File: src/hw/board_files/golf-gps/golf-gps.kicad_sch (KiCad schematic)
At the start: 33 parts, among them J1 Micro_SD_Card, J4 Conn_02x03_Top_Bottom, SW2 RESET, SW3 BTN_1, SW4 BTN_2, U1 NEO-M9N, U4 STM32L432KCU6, Y2 32.768kHz

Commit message: Added BOM file, finishing sch
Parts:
- removed C10: 2u2, symbol Device:C_Small
- removed C11, C16, C17, C8, C9: 100n, symbol Device:C_Small
- removed C12, C13: TBD, symbol Device:C_Small
- removed D2: LED_PWR, symbol Device:LED
- removed D4: LED_STATUS, symbol Device:LED
- removed J4: Conn_02x03_Top_Bottom, symbol Connector_Generic:Conn_02x03_Top_Bottom
- removed R11, R6: 330R, symbol Device:R_US
- removed R12, R13, R5: 10k, symbol Device:R_US
- removed SW2: RESET, symbol Switch:SW_Push
- removed SW3: BTN_1, symbol Switch:SW_Push
- removed SW4: BTN_2, symbol Switch:SW_Push
- removed U4: STM32L432KCU6, Package_DFN_QFN:QFN-32-1EP_5x5mm_P0.5mm_EP3.45x3.45mm, symbol MCU_ST_STM32L4:STM32L432KCUx
- removed Y2: 32.768kHz, symbol Device:Crystal_Small
- renumbered C3 to C1, C4 to C2, C2 to C3, J2 to J1, J1 to J2
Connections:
- net LCD_RES is gone; now on net +3V3: J1.4 (RES)
- net ANT: no longer names the net of AE1.1 (A), U1.11 (RF_IN)
- net V_BAT renamed V_BCKP
- no-connect marks 16 -> 9
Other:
- added sheet Microcontroller (microcontroller.kicad_sch)
- note added: "Golf GPS"
- note removed: "Add programming headers"
- note removed: "Buttons"
- note removed: "LEDs"
- note removed: "Pull high?"
- note removed: "STM32 Microcontroller"
- note removed: "SWD Programming Header"
- company: (none) -> Brady Kuhn
- title: (none) -> Golf GPS

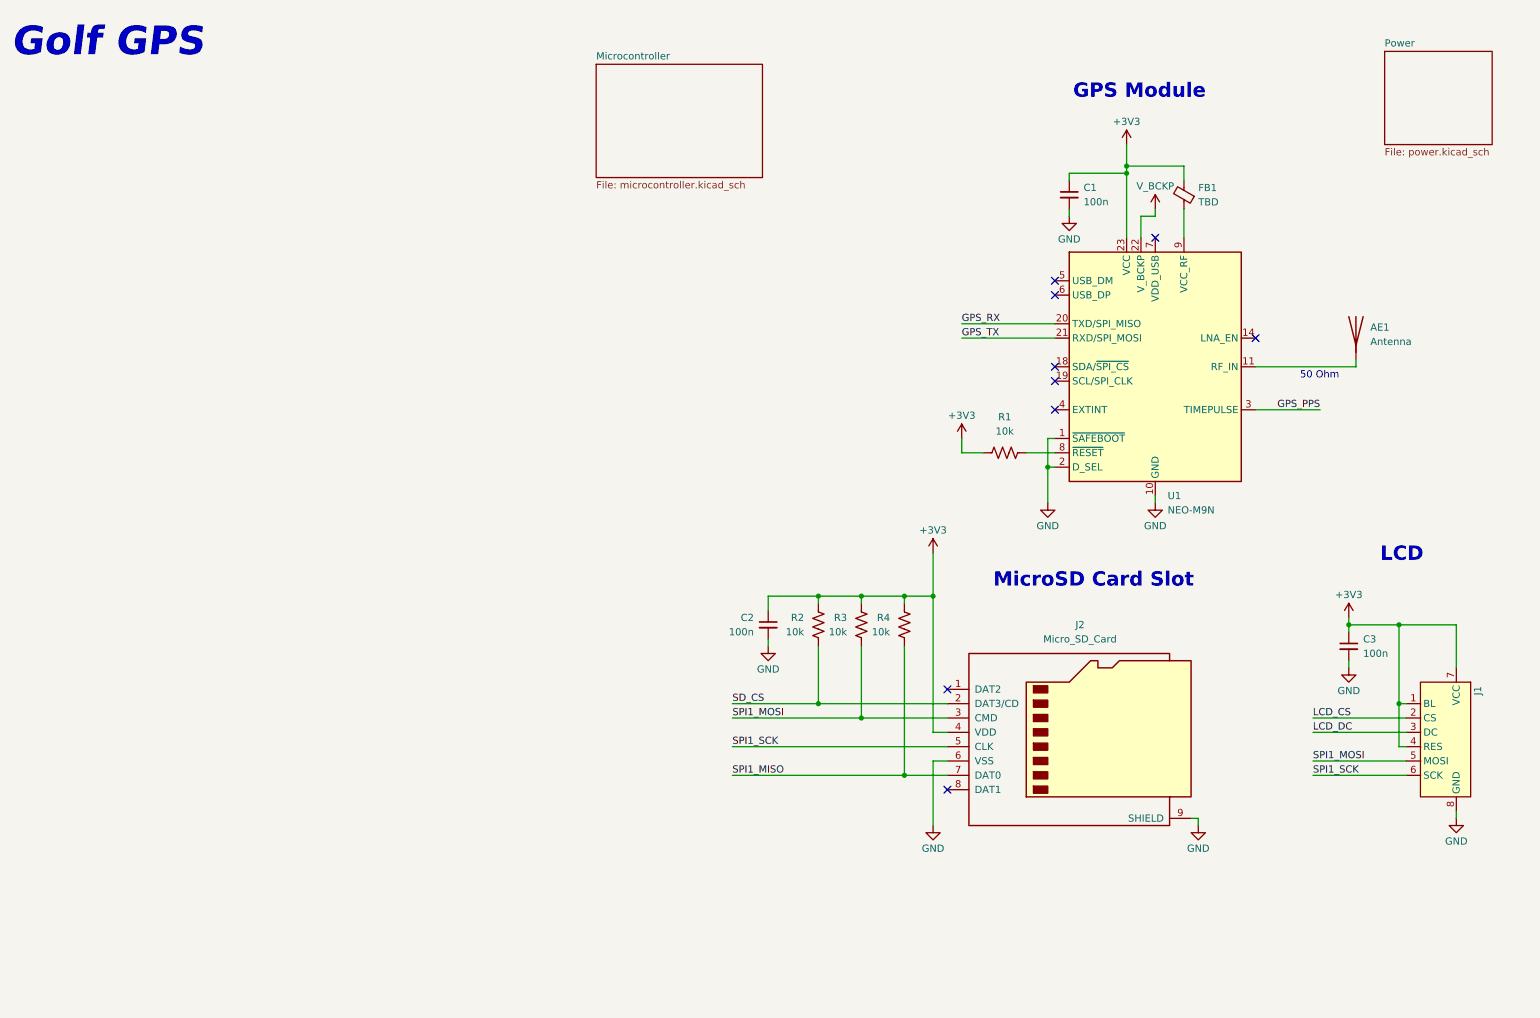
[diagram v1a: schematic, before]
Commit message: Added PI filter to antenna.
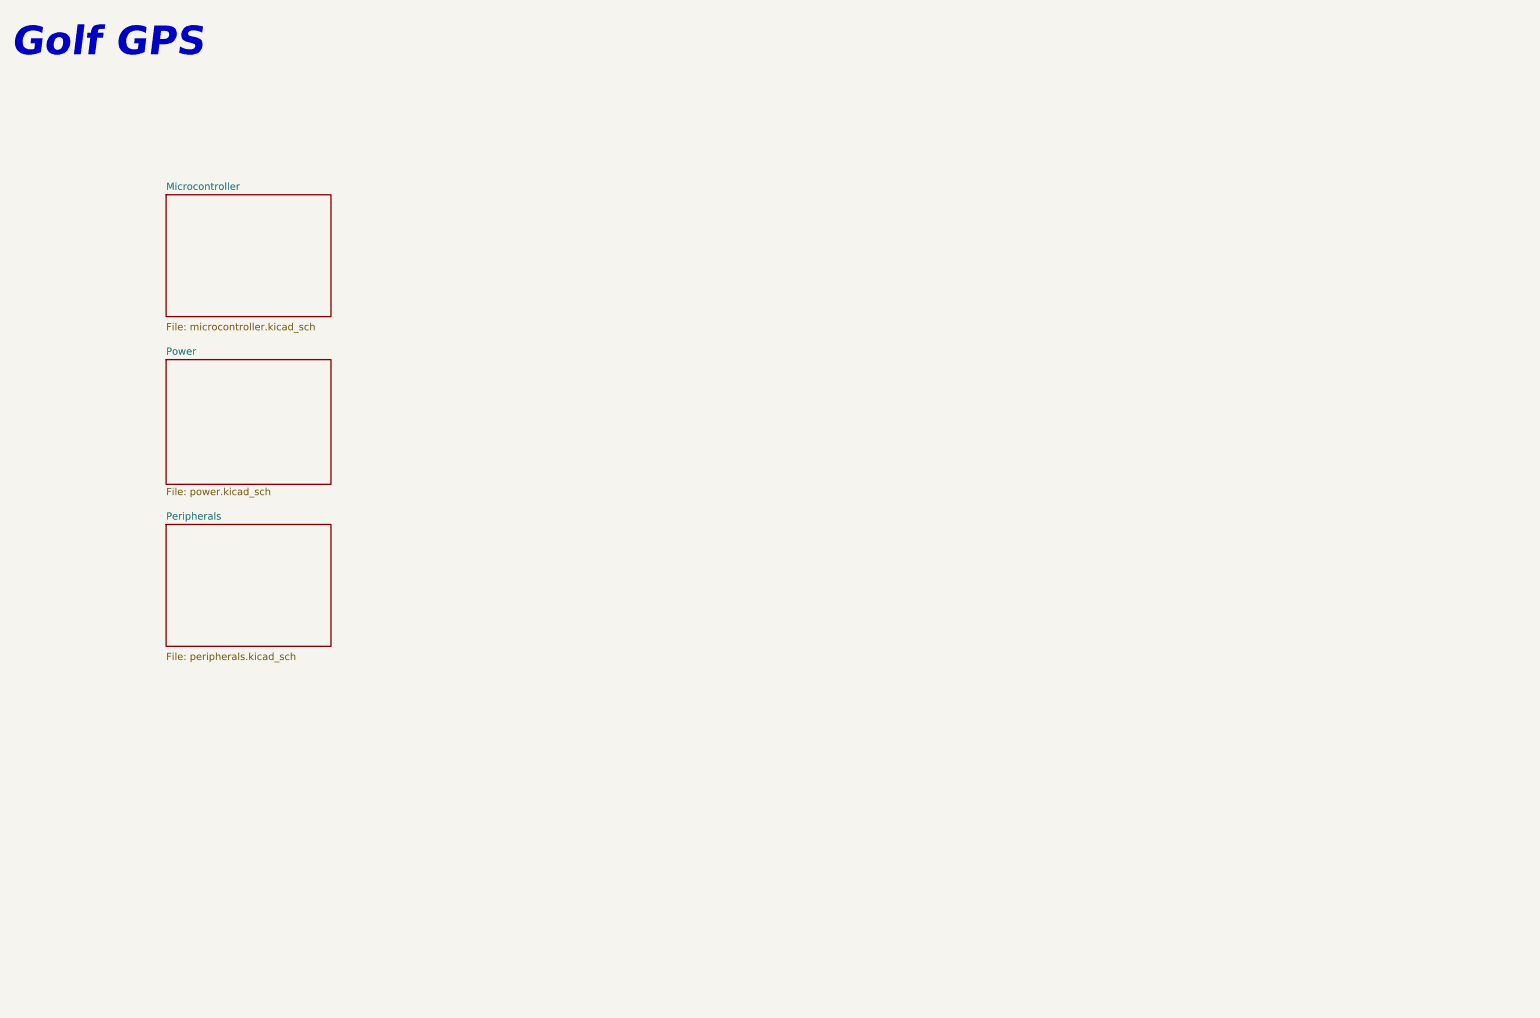
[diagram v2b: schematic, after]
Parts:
- removed AE1: Antenna, symbol Device:Antenna
- removed C1, C2, C3: 100n, symbol Device:C_Small
- removed FB1: TBD, symbol Device:FerriteBead_Small
- removed J1: ~, Connector_PinSocket_2.54mm:PinSocket_1x08_P2.54mm_Vertical, symbol Headers:9-pin_LCD_header
- removed J2: Micro_SD_Card, symbol Connector:Micro_SD_Card
- removed R1, R2, R3, R4: 10k, symbol Device:R_US
- removed U1: NEO-M9N, RF_GPS:ublox_NEO, symbol RF_GPS:NEO-M9N
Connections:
- no-connect marks 9 -> 0
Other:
- added sheet Peripherals (peripherals.kicad_sch)
- note removed: "50 Ohm"
- note removed: "GPS Module"
- note removed: "LCD"
- note removed: "MicroSD Card Slot"

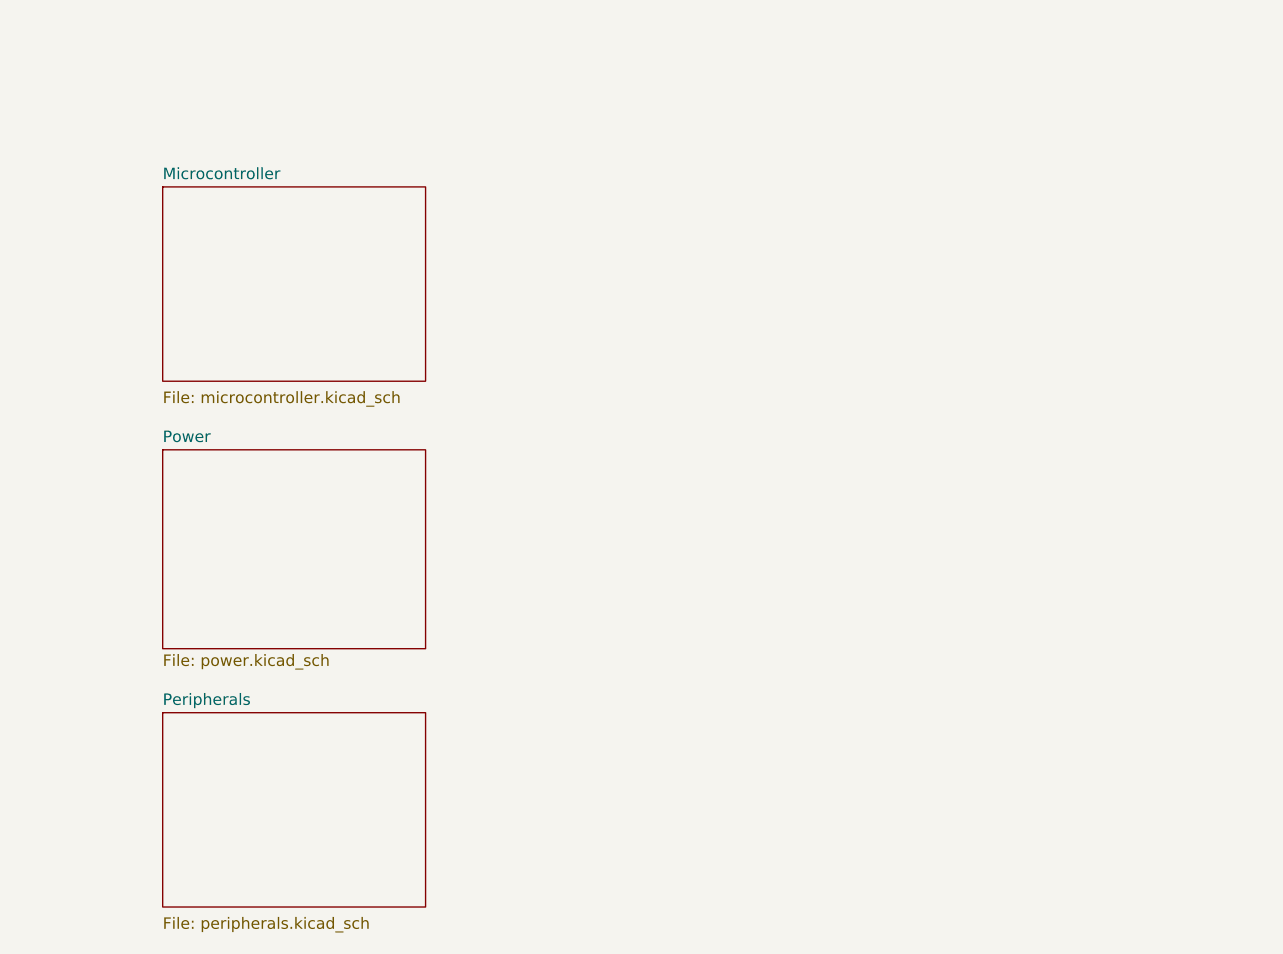
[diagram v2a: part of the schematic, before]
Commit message: Finished sch, started power section on PCB
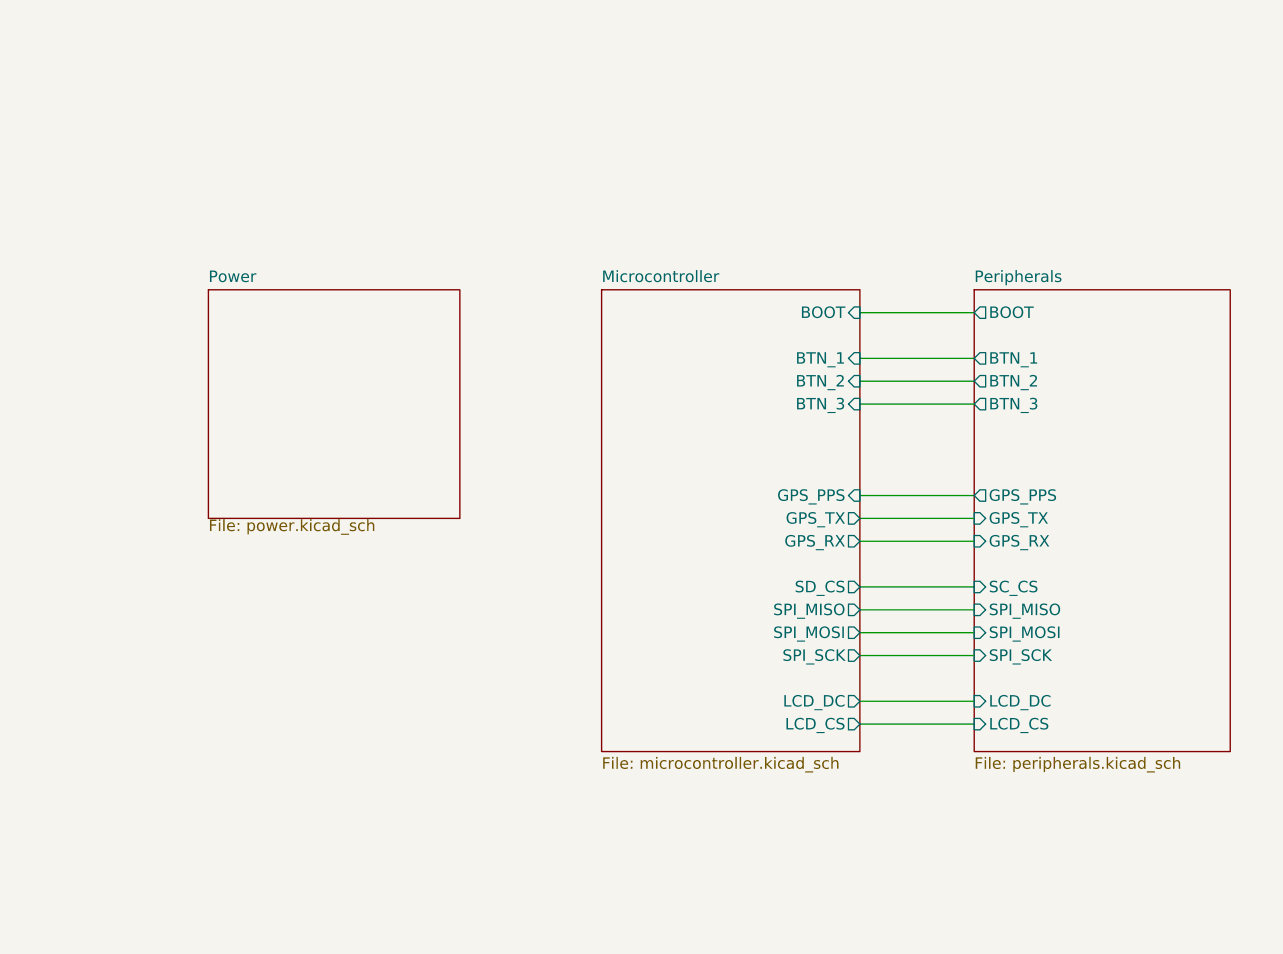
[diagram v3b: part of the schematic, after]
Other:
- sheet Microcontroller ports: added BOOT, BTN_1, BTN_2, BTN_3, GPS_PPS, GPS_RX, GPS_TX, LCD_CS, LCD_DC, SD_CS, SPI_MISO, SPI_MOSI, SPI_SCK; removed none
- sheet Peripherals ports: added BOOT, BTN_1, BTN_2, BTN_3, GPS_PPS, GPS_RX, GPS_TX, LCD_CS, LCD_DC, SC_CS, SPI_MISO, SPI_MOSI, SPI_SCK; removed none
- company: Brady Kuhn -> B. Kuhn

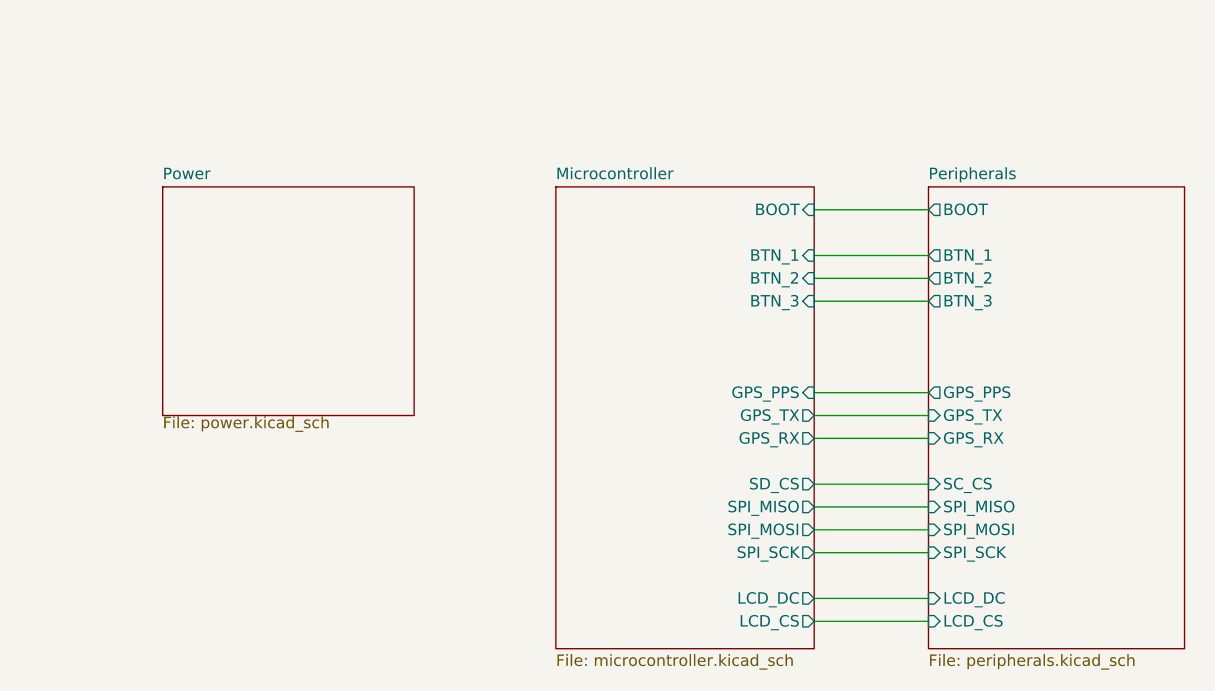
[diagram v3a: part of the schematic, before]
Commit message: Finished new sch. Updated pinout. Started new PCB.
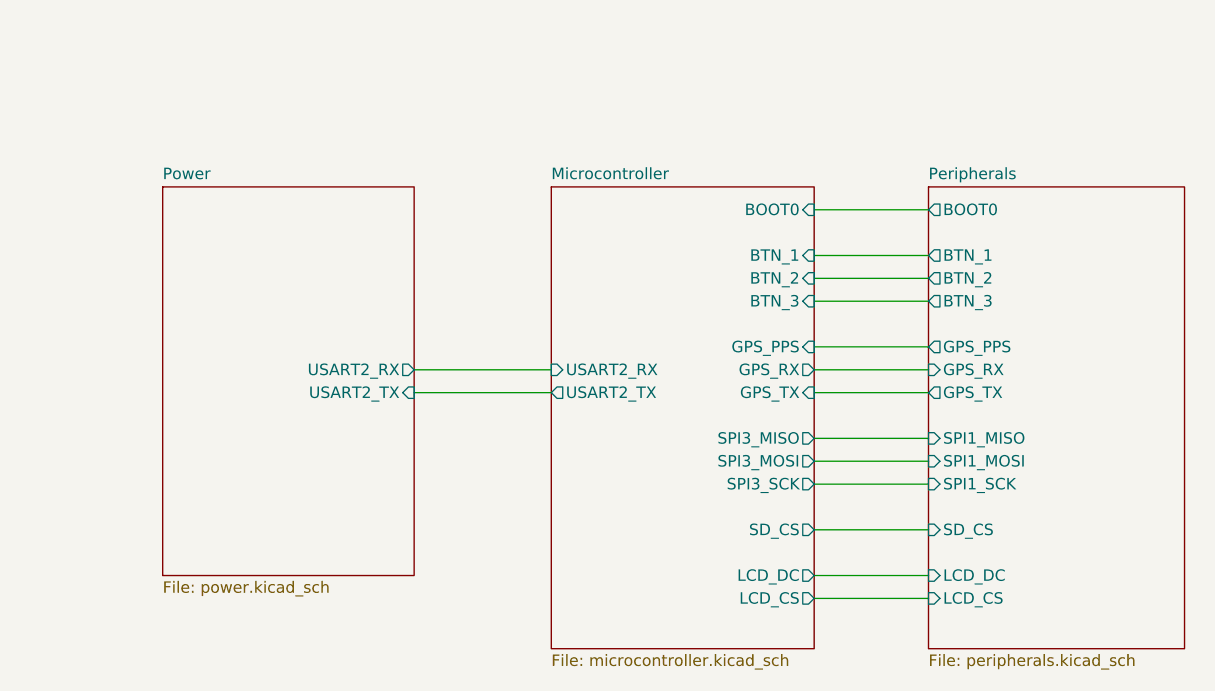
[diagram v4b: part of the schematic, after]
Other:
- sheet Microcontroller ports: added BOOT0, SPI3_MISO, SPI3_MOSI, SPI3_SCK, USART2_RX, USART2_TX; removed BOOT, SPI_MISO, SPI_MOSI, SPI_SCK
- sheet Peripherals ports: added BOOT0, SD_CS, SPI1_MISO, SPI1_MOSI, SPI1_SCK; removed BOOT, SC_CS, SPI_MISO, SPI_MOSI, SPI_SCK
- sheet Power ports: added USART2_RX, USART2_TX; removed none
